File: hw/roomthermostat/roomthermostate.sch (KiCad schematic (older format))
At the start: 0 parts

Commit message: common shared schematics, buscom schematics and roomthermostate schematics added.
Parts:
- added C? (x7): 100nF, symbol C
- added C? (x2): 18pF, symbol C
- added C? (x4): 4,7nF, symbol C
- added C? (x8): 1uF, 0805, symbol C
- added D?: 1N4148, symbol D
- added J?: JUMPER, symbol JUMPER
- added J?: CONN_6X1, symbol CONN_6X1
- added J?: CONN_4X1, symbol CONN_4X1
- added J? (x2): CONN_3X1, symbol CONN_3X1
- added L?: L, symbol L
- added Q?: BC846, SOT23_21-3, symbol BC846
- added R? (x6): 4,7k, symbol R
- added R? (x2): 1,6, symbol R
- added R? (x8): 1k, symbol R
- added R? (x3): 470k, symbol R
- added U?: ATMEGA324-TQFP44, TQFP44, symbol ATMEGA324-TQFP44
- added U?: 7,3728MHz, symbol CRYSTAL
- added U?: EA-DOGM-132-XX, symbol EA-DOGM-132-XX
- added U?: 25LCXXX, SO8N, symbol 25LCXXX
- added U?: TSIC306_TO92, TO92, symbol TSIC306_TO92
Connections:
- net labels added: CS_EEP, CS_LCD, EXT_SW0, EXT_SW1, GND, LCD_A0, LCD_LED, MISO, MOSI, QTAIN0, QTSCL, QTSDA, QTSMP, QTX0, QTX1, QTX2, QTY0A, QTY0B, QTY1A, QTY1B, QTY2A, QTY2B, RESET, SCK, TEMP, VCC
- wire segments 0 -> 211
- no-connect marks 0 -> 6
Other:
- note added: "Display"
- note added: "External switches for windows\nand sabotage contacts"
- note added: "Program EEProm"
- note added: "QTouch AIN0\n"
- note added: "QTouch Matrix for user interface\n(up to 9 buttons)"
- note added: "QTouch SMP"
- note added: "QTouch TWI Debug Port SCL"
- note added: "QTouch TWI Debug Port SDA"
- note added: "QTouch X0"
- note added: "QTouch X1"
- note added: "QTouch X2"
- note added: "QTouch Y0A"
- note added: "QTouch Y0B"
- note added: "QTouch Y1A"
- note added: "QTouch Y1B"
- note added: "QTouch Y2A"
- note added: "QTouch Y2B"
- note added: "Temperature Sensor"

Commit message: updated businterface
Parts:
- removed C? (x3): 4,7nF, symbol C
- removed J?: CONN_4X1, symbol CONN_4X1
- removed J? (x2): CONN_3X1, symbol CONN_3X1
- removed R? (x6): 1k, symbol R
- removed R? (x3): 470k, symbol R
- added C? (x3): 4,7nF, symbol C
- added J? (x4): CONN_1, symbol CONN_1
- added J?: CONN_5X1, symbol CONN_5X1
- added J? (x2): CONN_10X1, symbol CONN_10X1
- added R? (x3): 4,7k, symbol R
- R? (x2): value 1,6 -> 3,3
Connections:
- net labels added: PA6, PA7, PB0, PB1, PC2, PC3, PC4, PC5, PC6, PC7, PD3, QTSNS0, QTSNS1, QTSNS2, QTSNS3, QTSNSK0, QTSNSK1, QTSNSK2, QTSNSK3
- net labels removed: QTAIN0, QTSMP, QTX0, QTX1, QTX2, QTY0A, QTY0B, QTY1A, QTY1B, QTY2A, QTY2B
- wire segments 211 -> 218
- no-connect marks 6 -> 5
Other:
- note added: "JTAG"
- note added: "JTAG Pin 1"
- note added: "JTAG Pin 3"
- note added: "JTAG Pin 5"
- note added: "JTAG Pin 9"
- note added: "Pin Reste-Rampe"
- note added: "QTouch Button 0 "-""
- note added: "QTouch Button 1 "Menu/OK""
- note added: "QTouch Button 2 "+""
- note added: "QTouch Button 3 "Reserve""
- note added: "QTouch buttons for user interface"
- note added: "TCK"
- note added: "TDI"
- note added: "TDO"
- note added: "TMS"
- note removed: "QTouch AIN0\n"
- note removed: "QTouch Matrix for user interface\n(up to 9 buttons)"
- note removed: "QTouch SMP"
- note removed: "QTouch X0"
- note removed: "QTouch X1"
- note removed: "QTouch X2"
- note removed: "QTouch Y0A"
- note removed: "QTouch Y0B"
- note removed: "QTouch Y1A"
- note removed: "QTouch Y1B"
- note removed: "QTouch Y2A"
- note removed: "QTouch Y2B"

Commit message: - updated roomthermostate schematics - added hardware README
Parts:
- added C7: 100nF, symbol C
- gave numbers to parts that had none: 51
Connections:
- net GND: now also C7.2
- net VCC: now also C7.1

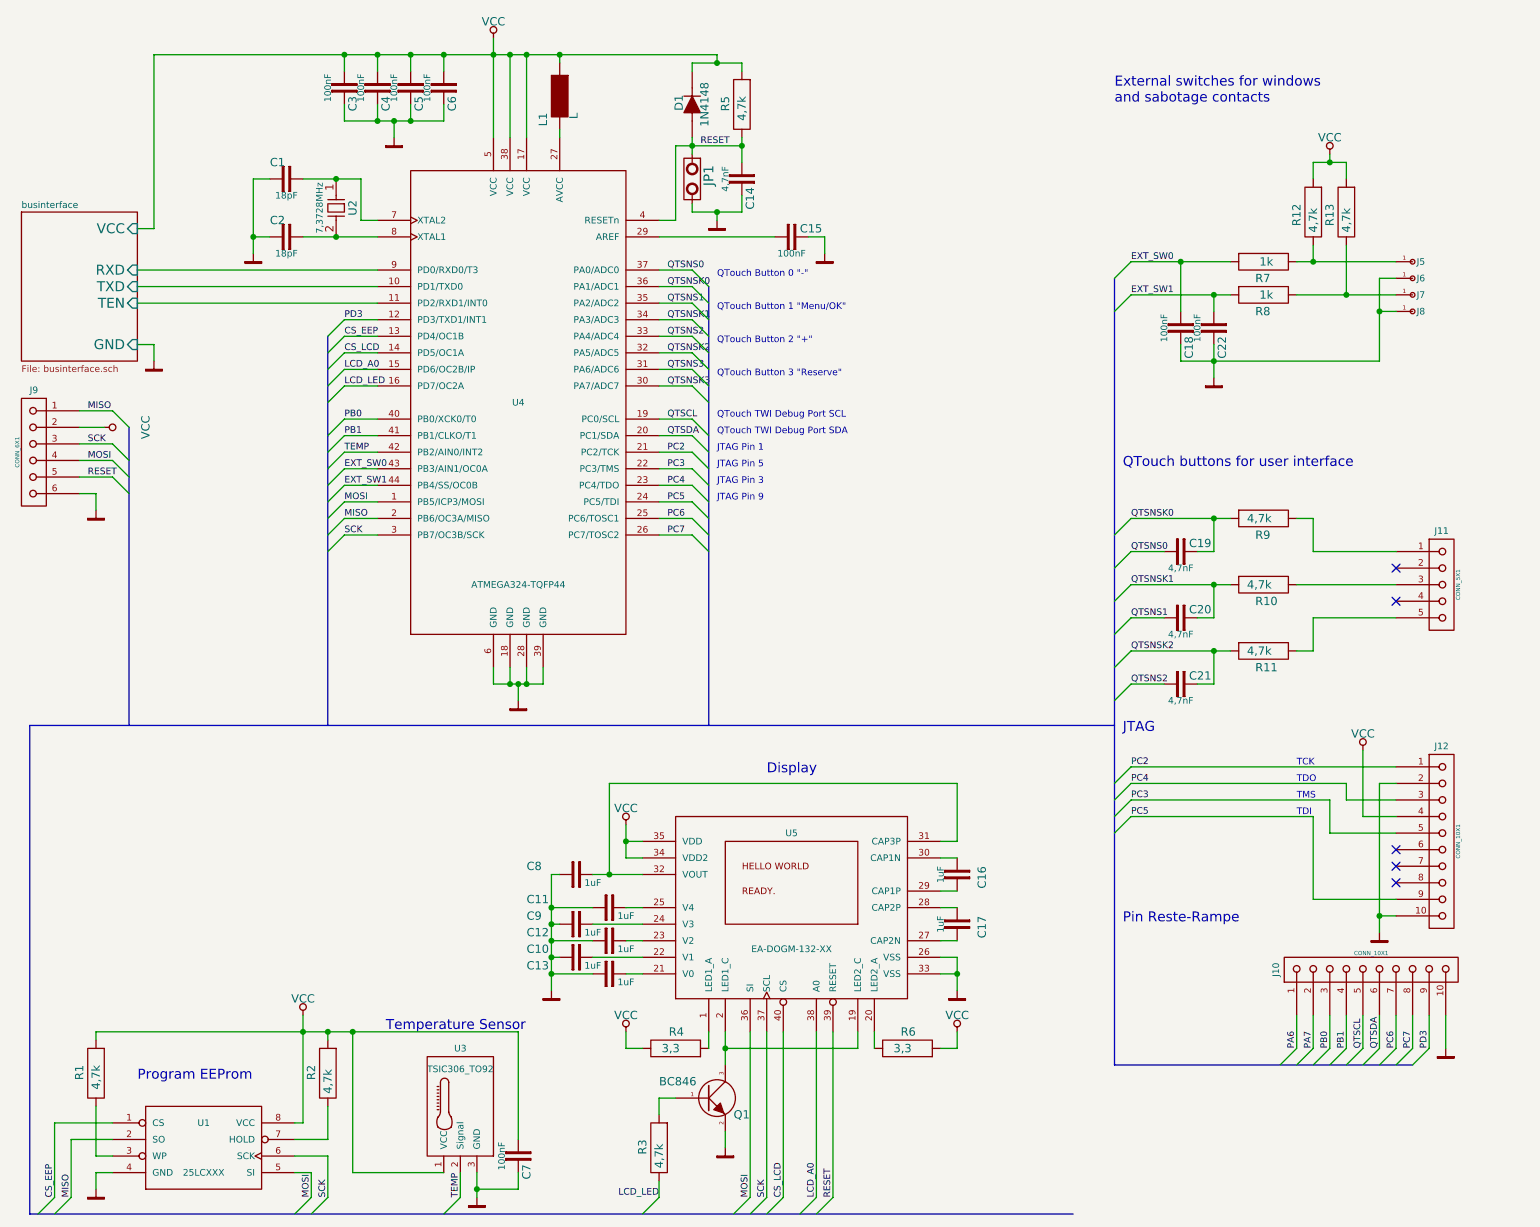
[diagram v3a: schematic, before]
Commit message: further drawing of roomthermostate schematics and footprint selection
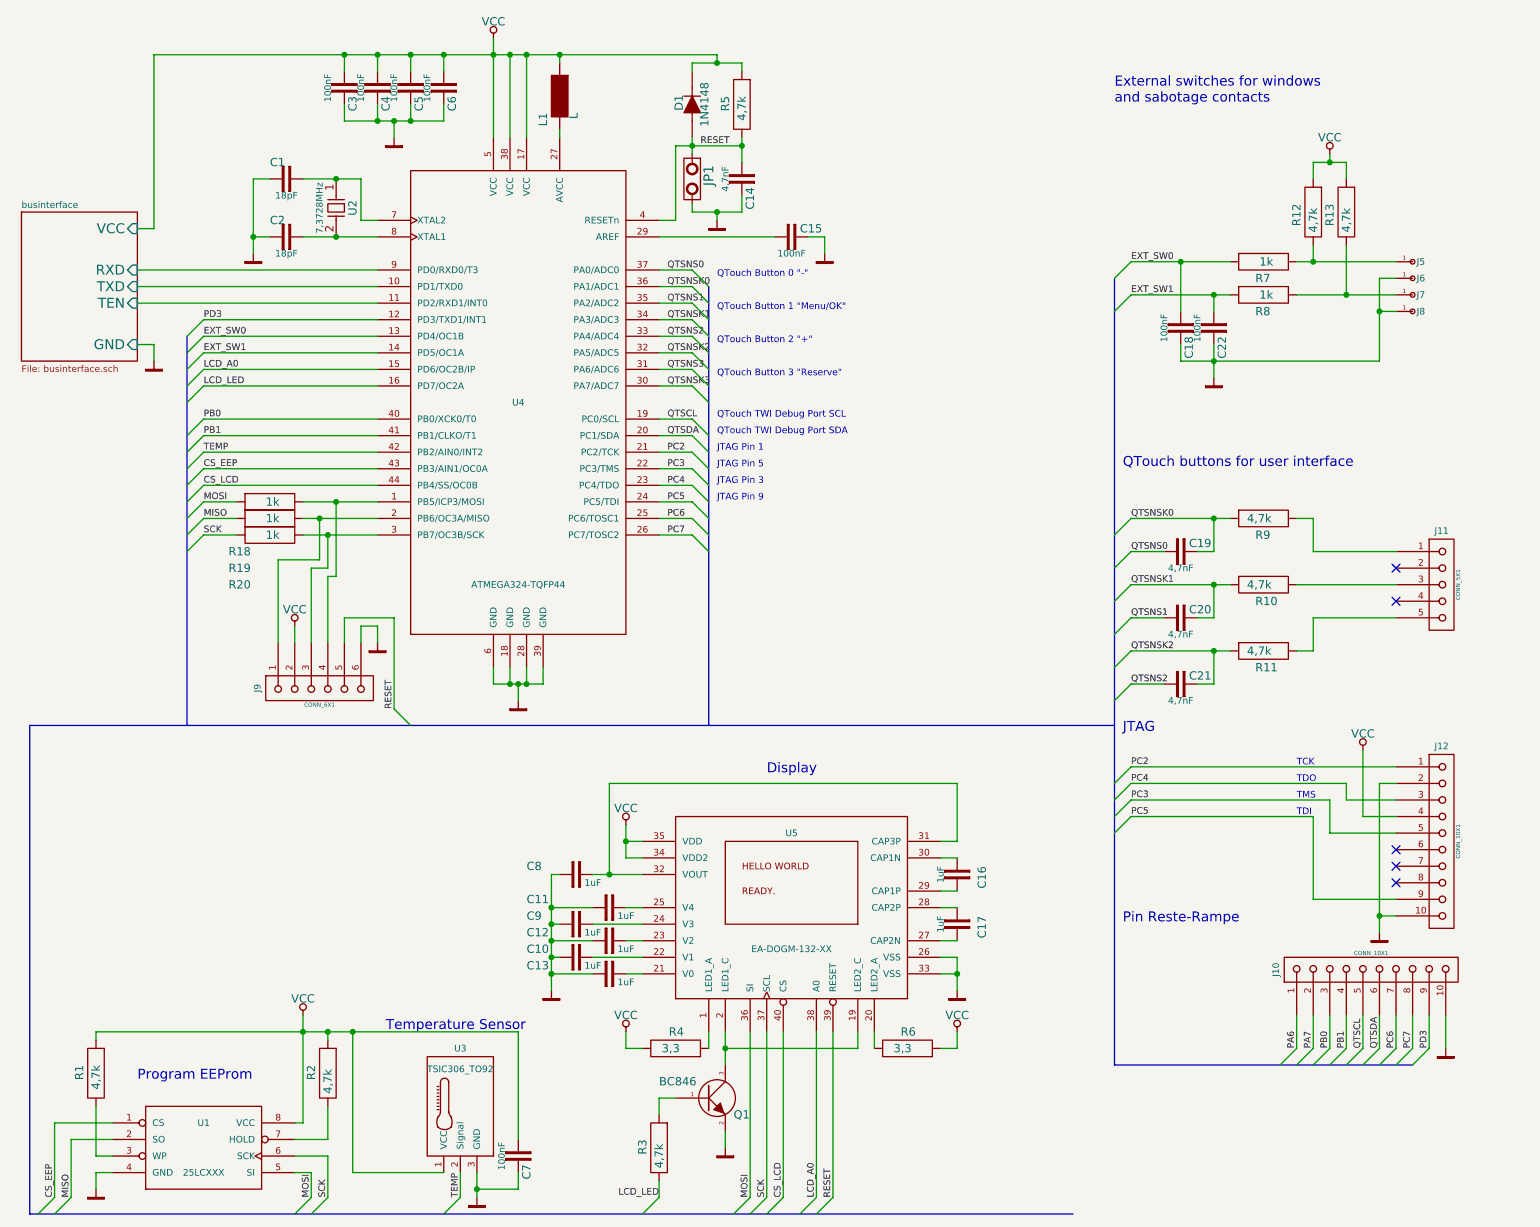
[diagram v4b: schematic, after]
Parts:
- added R18, R19, R20: 1k, symbol R
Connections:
- net CS_EEP: now also U4.43 (PB3/AIN1/OC0A); no longer U4.13 (PD4/OC1B)
- net CS_LCD: now also U4.44 (PB4/SS/OC0B); no longer U4.14 (PD5/OC1A)
- net EXT_SW0: now also U4.13 (PD4/OC1B); no longer U4.43 (PB3/AIN1/OC0A)
- net EXT_SW1: now also U4.14 (PD5/OC1A); no longer U4.44 (PB4/SS/OC0B)
- net MISO: now also R19.1; no longer J9.1, U4.2 (PB6/OC3A/MISO)
- net MOSI: now also R18.1; no longer J9.4, U4.1 (PB5/ICP3/MOSI)
- net SCK: now also R20.1; no longer J9.3, U4.3 (PB7/OC3B/SCK)
- new net: J9.4, R18.2, U4.1 (PB5/ICP3/MOSI)
- new net: J9.1, R19.2, U4.2 (PB6/OC3A/MISO)
- new net: J9.3, R20.2, U4.3 (PB7/OC3B/SCK)
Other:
- moved on the sheet: J9

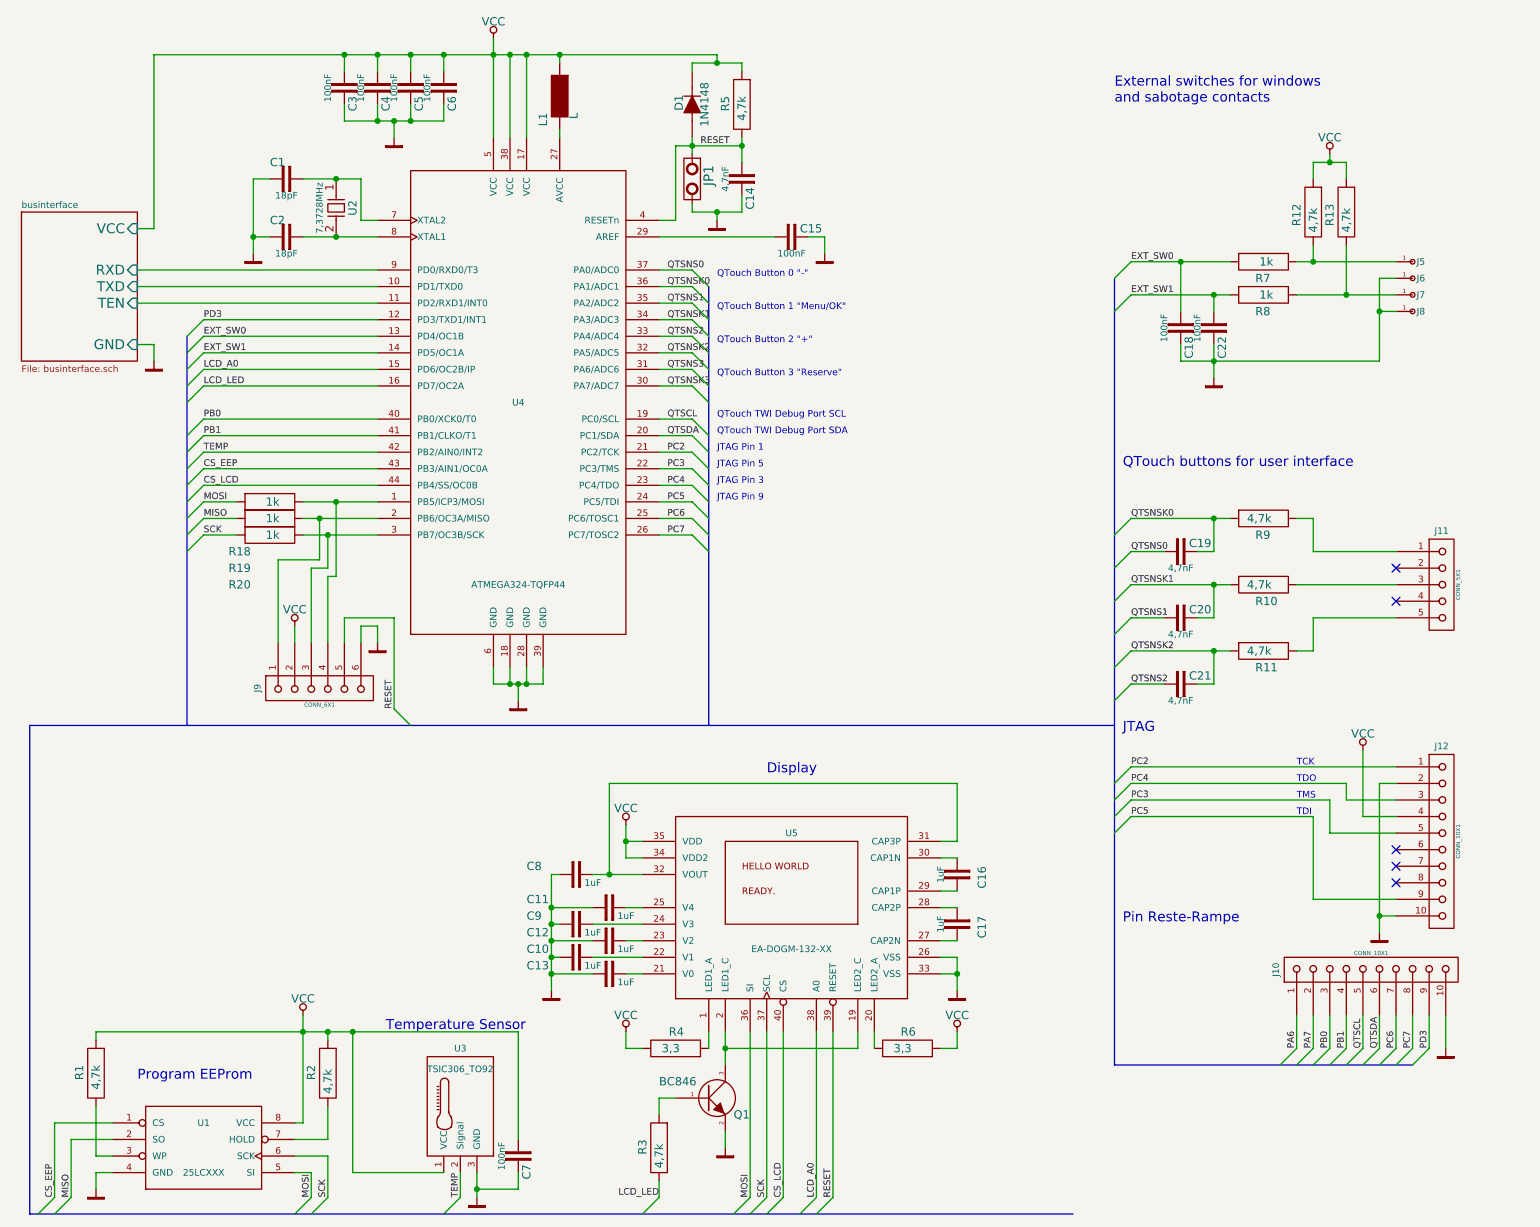
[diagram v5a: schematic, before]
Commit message: Schematic changes: - TXEN now on PD4 - Temperature sensor power is switchable - LCD Reset added - CS of EEP and LCD switched
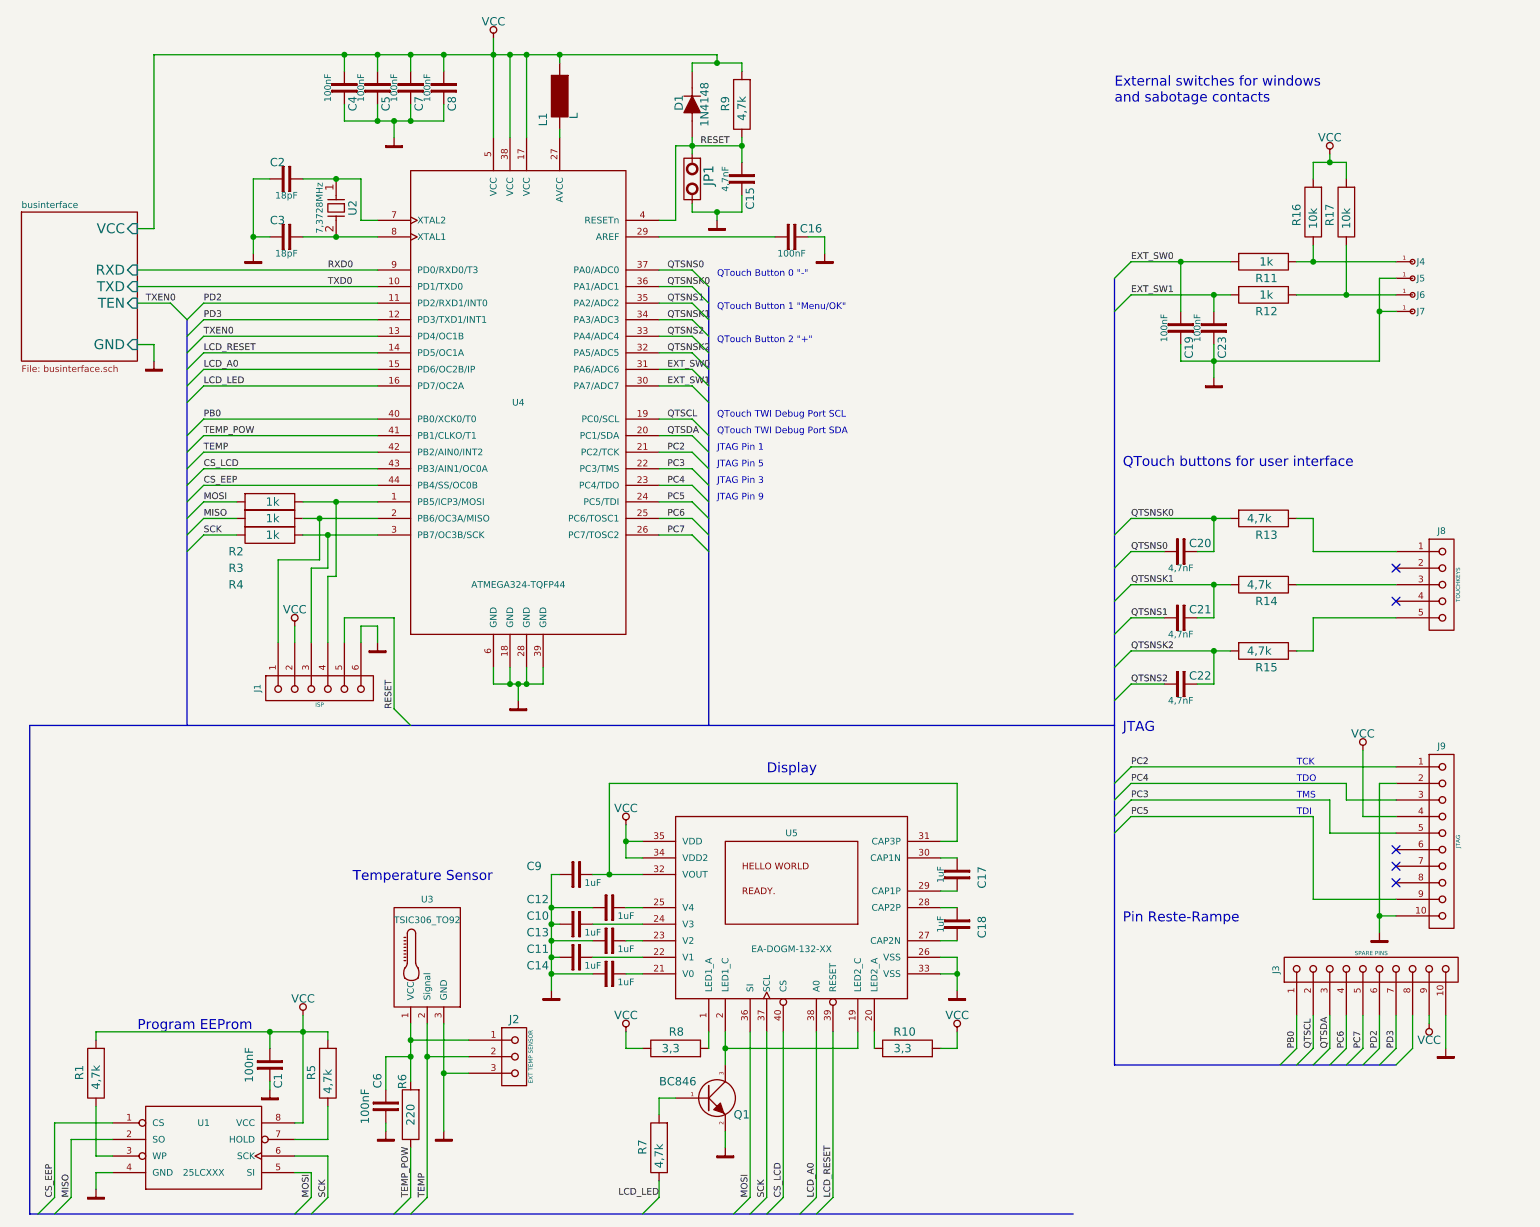
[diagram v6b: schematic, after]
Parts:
- removed C7: 100nF, symbol C
- added C1, C6: 100nF, symbol C
- added J2: EXT TEMP SENSOR, symbol CONN_3X1
- added R6: 220, symbol R
- J1: renamed from J9; value CONN_6X1 -> ISP
- J3: renamed from J10; value CONN_10X1 -> SPARE PINS
- J4: renamed from J5; value CONN_1 -> EXT SWITCH 1 SIGNAL
- J5: renamed from J6; value CONN_1 -> EXT SWITCH 1 GND
- J6: renamed from J7; value CONN_1 -> EXT SWITCH 2 SIGNAL
- J7: renamed from J8; value CONN_1 -> EXT SWITCH 2 GND
- J8: renamed from J11; value CONN_5X1 -> TOUCHKEYS
- J9: renamed from J12; value CONN_10X1 -> JTAG
- R16: renamed from R12; value 4,7k -> 10k
- R17: renamed from R13; value 4,7k -> 10k
- renumbered C9 to C10, C10 to C11, C11 to C12, C12 to C13, C13 to C14, C14 to C15, C15 to C16, C16 to C17, C17 to C18, C18 to C19, C1 to C2, C19 to C20, C20 to C21, C21 to C22, C22 to C23, C2 to C3, C3 to C4, C4 to C5, C5 to C7, C6 to C8, C8 to C9, R6 to R10, R7 to R11, R8 to R12, R9 to R13, R10 to R14, R11 to R15, R18 to R2, R19 to R3, R20 to R4, R2 to R5, R3 to R7, R4 to R8, R5 to R9
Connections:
- net PA6 is gone; now on net PB0: J3.1
- net PA7 is gone; now on net QTSCL: J3.2
- net QTSNS3 is gone; now on net EXT_SW0: U4.31 (PA6/ADC6)
- net QTSNSK3 is gone; now on net EXT_SW1: U4.30 (PA7/ADC7)
- net CS_EEP: now also U4.44 (PB4/SS/OC0B); no longer U4.43 (PB3/AIN1/OC0A)
- net CS_LCD: now also U4.43 (PB3/AIN1/OC0A); no longer U4.44 (PB4/SS/OC0B)
- net EXT_SW0: no longer U4.13 (PD4/OC1B)
- net EXT_SW1: no longer U4.14 (PD5/OC1A)
- net GND: now also C1.2, C6.2, J2.3
- net PB0: no longer J3.3
- net PC6: now also J3.4; no longer J3.7
- net PC7: now also J3.5; no longer J3.8
- net PD3: now also J3.7; no longer J3.9
- net QTSCL: no longer J3.5
- net QTSDA: now also J3.3; no longer J3.6
- net RESET: no longer U5.39 (RESET)
- net TEMP: now also J2.2
- net VCC: now also J3.9, C1.1; no longer U3.1 (VCC)
- net PB1 renamed TEMP_POW
- net TEMP_POW: now also R6.2; no longer J3.4
- net businterface/RXD renamed RXD0
- net businterface/TEN renamed PD2
- net PD2: now also J3.6
- net businterface/TXD renamed TXD0
- new net: C6.1, J2.1, R6.1, U3.1 (VCC)
- new net LCD_RESET: U4.14 (PD5/OC1A), U5.39 (RESET)
- new net TXEN0: U4.13 (PD4/OC1B)
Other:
- note removed: "QTouch Button 3 "Reserve""
- moved on the sheet: U3
